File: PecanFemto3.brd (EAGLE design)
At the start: 16.6 x 21.2 mm, 29 parts

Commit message: Added step down converter
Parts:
- added L2: 33uH, PecanPico6:LPS3015
- added L3: 10uH, PecanPico6:LPS3015
- added U$26: 10uF, sven:0805
- added U$27: 100nF, sven:0402
- added U1: TPS62203DBVT, TPS62203:SOT95P280X145-5N
- U$23: value 10uH -> 2.2uF; device PecanPico6:LPS3015 -> sven:0603
- moved U$23 6.59 mm to (13.9, 17.1)
- moved U$14 1.20 mm to (16.4, 15.6)
- moved U$22 0.80 mm to (15.4, 15.6)
- moved U$24 0.61 mm to (11.9, 17.8), turned to 270 degrees
- moved U$16 0.50 mm to (15.7, 17.3)
- moved U$13 0.40 mm to (11.6, 17.9)
- moved U$5 0.10 mm to (13.0, 13.1)
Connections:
- new net N$1: U$23.P$1, U$3.8/V_BCKP
- new net N$15: L3.1_1, L3.1_2, L3.1_3, L3.1_4, L3.1_5, L3.1_6, L3.1_7, L3.1_8, L3.1_9, U1.5
- new net VCC_EN: U$4.16, U1.3
- net GND: now also U$26.P$1, U$27.P$1, U1.2
- net N$14: now also L2.1_1, L2.1_2, L2.1_3, L2.1_4, L2.1_5, L2.1_6, L2.1_7, L2.1_8, L2.1_9; no longer U$23.1_1, U$23.1_2, U$23.1_3, U$23.1_4, U$23.1_5, U$23.1_6, U$23.1_7, U$23.1_8, U$23.1_9
- net VBAT: now also JP1.1, U$23.P$2, U$27.P$2, U$4.19, U1.1
- net VCC: now also L3.2_1, L3.2_2, L3.2_3, L3.2_4, L3.2_5, L3.2_6, L3.2_7, L3.2_8, L3.2_9, U$26.P$2, U1.4; no longer JP1.1, U$3.8/V_BCKP, U$4.19
- net VSOLAR: now also L2.2_1, L2.2_2, L2.2_3, L2.2_4, L2.2_5, L2.2_6, L2.2_7, L2.2_8, L2.2_9; no longer U$23.2_1, U$23.2_2, U$23.2_3, U$23.2_4, U$23.2_5, U$23.2_6, U$23.2_7, U$23.2_8, U$23.2_9
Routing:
- net VCC: track 54.2 -> 38.3 mm
- net VCC_EN: track 0.00 -> 8.71 mm
- net N$15: track 0.00 -> 6.32 mm, vias 0 -> 1
- net VBAT: track 21.0 -> 24.2 mm
- net N$1: track 0.00 -> 1.89 mm
- net VSOLAR: track 26.2 -> 25.4 mm

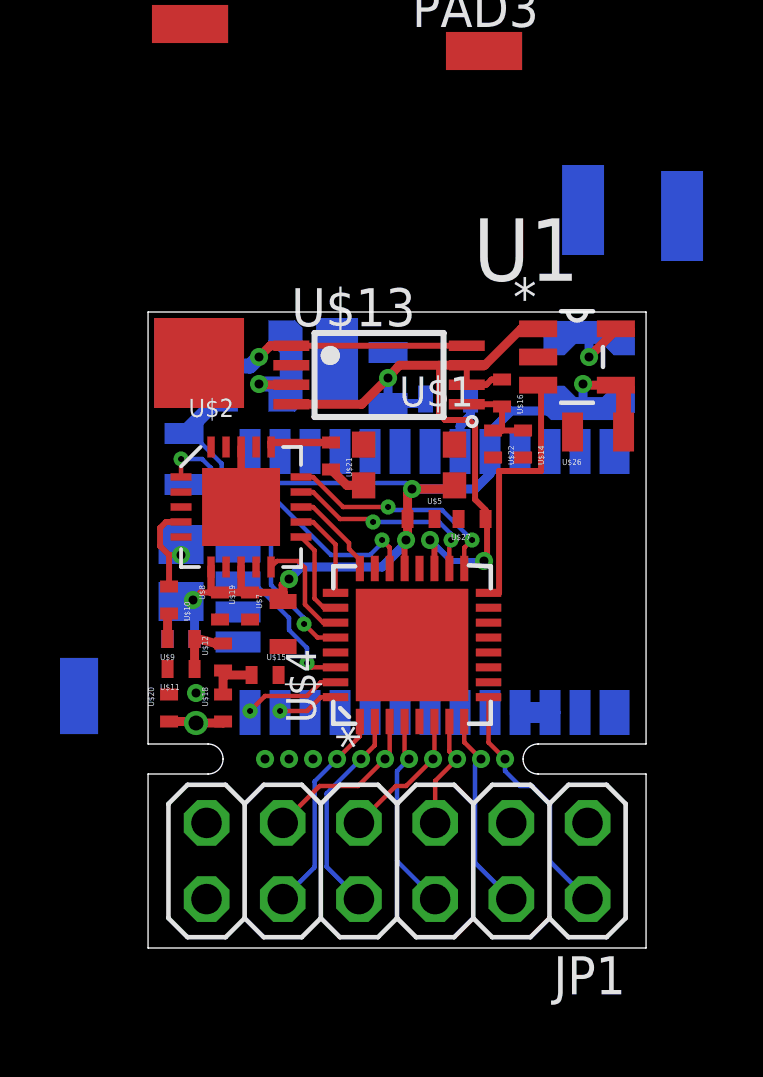
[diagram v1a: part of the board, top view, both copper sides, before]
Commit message: Moved components around
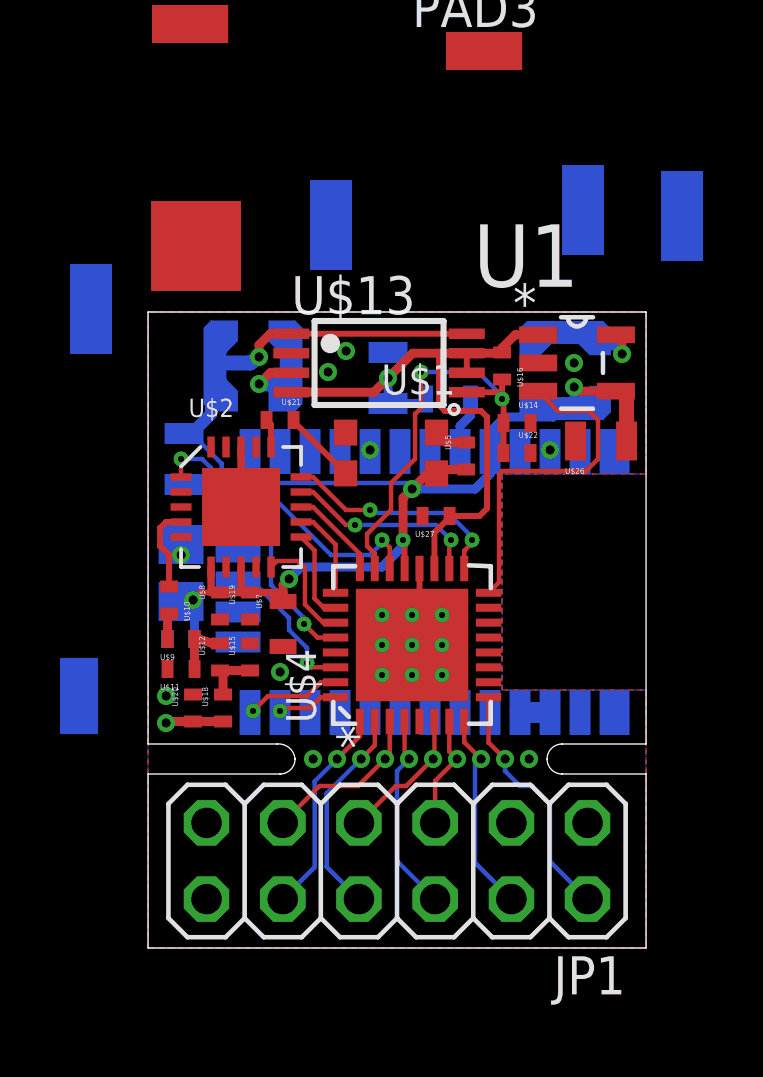
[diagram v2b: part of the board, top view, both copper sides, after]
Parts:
- moved U$5 2.58 mm to (14.5, 15.2), turned to 270 degrees
- moved U$21 2.08 mm to (8.30, 16.4), turned to 180 degrees
- moved U$27 1.20 mm to (13.5, 13.2)
- moved U$16 0.90 mm to (15.7, 18.2)
- moved U$22 0.85 mm to (16.2, 15.3), turned to 180 degrees
- moved L3 0.80 mm to (17.8, 18.1)
- moved U$20 0.80 mm to (5.40, 6.80)
- moved U$15 0.78 mm to (7.30, 8.50), turned to 270 degrees
- moved U$14 0.73 mm to (16.2, 16.3), turned to 180 degrees
- moved U$1 0.72 mm to (12.0, 15.3)
- moved U$13 0.40 mm to (11.6, 18.3)
- moved U$26 0.32 mm to (19.0, 15.7)
- moved U1 0.20 mm to (18.2, 18.3)
- moved U$12 0.10 mm to (6.30, 8.50)
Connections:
- removed net N$17: U$13.5, U$14.P$2, U$16.P$1, U$22.P$2
- new net VBAT_DIFF: U$13.5, U$14.P$2, U$16.P$1, U$22.P$2, U$4.23
- net VBAT: no longer U$4.23
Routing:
- net VBAT_DIFF: track 0.00 -> 14.2 mm, vias 0 -> 2
- net VCC: track 38.3 -> 41.4 mm
- net N$17: track 3.11 -> 0.00 mm
- net GND: track 2.00 -> 4.92 mm, vias 4 -> 18
- net VCC_EN: track 8.71 -> 11.3 mm
- net VBAT: track 24.2 -> 21.8 mm, vias 3 -> 1
- net N$9: track 1.30 -> 2.50 mm
- net N$10: track 2.15 -> 0.96 mm
- net VSOLAR: track 25.4 -> 24.4 mm
- net N$15: track 6.32 -> 6.86 mm
- added copper zone on layer 1, net GND
- added copper zone on layer 16, net GND
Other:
- outline, holes or cut-outs redrawn

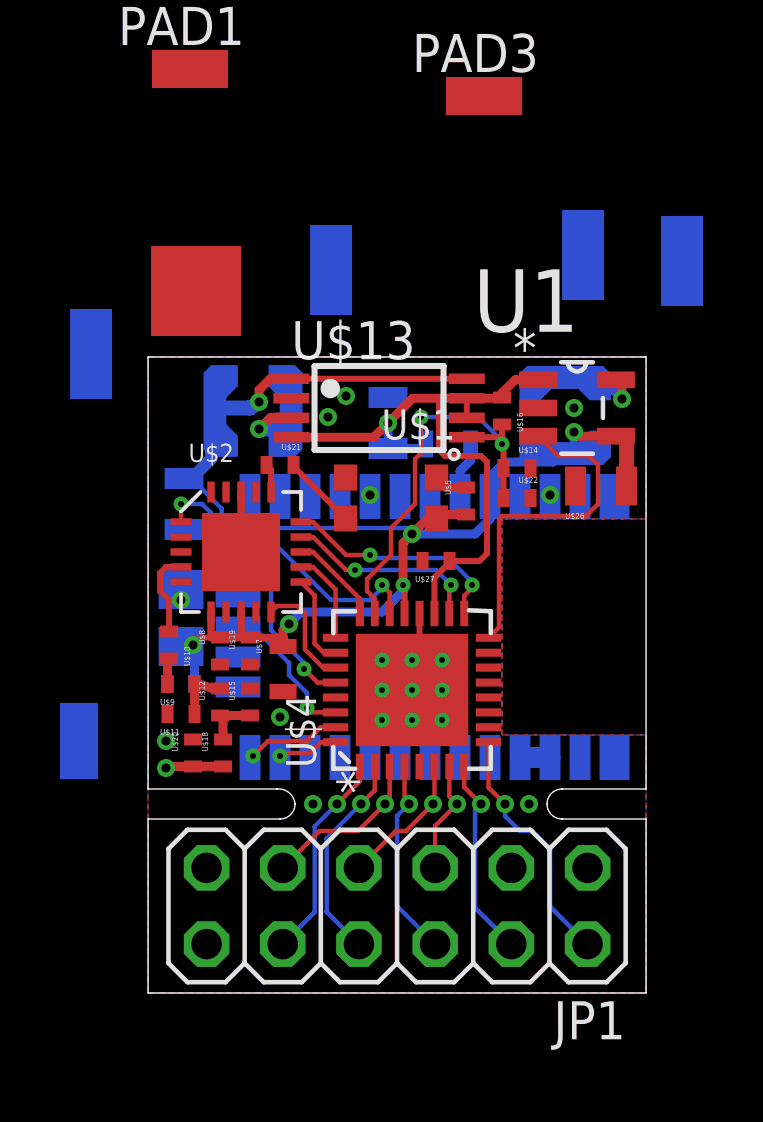
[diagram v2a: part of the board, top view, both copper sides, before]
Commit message: Moved parts around
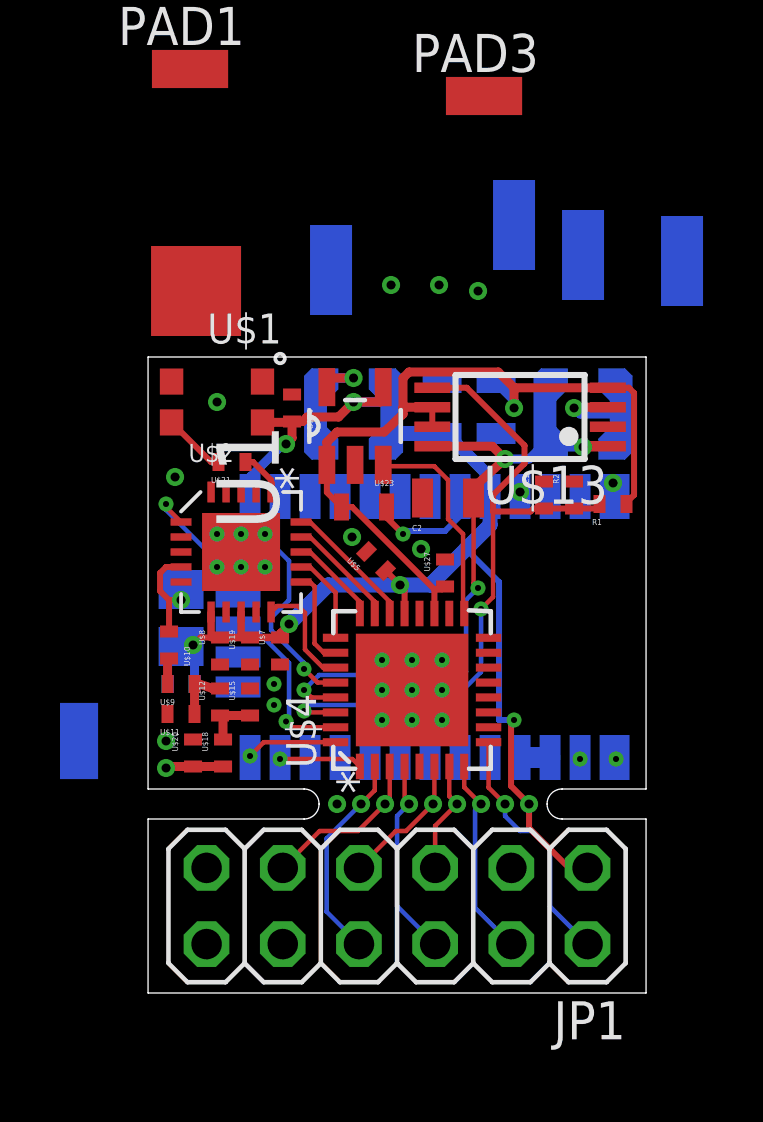
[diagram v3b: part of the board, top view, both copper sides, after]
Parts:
- removed U$16: 22k, PecanPico6:0402
- removed U$17: 22uF, sven:0805
- removed U$22: 10k, PecanPico6:0402
- removed U$24, U$26: 10uF, sven:0805
- added C1: 1nF, sven:0402
- added C2: 22uF, sven:0805
- added C3, C4: 10uF, sven:0805
- added R1: 22k, PecanPico6:0402
- added R2: 10k, PecanPico6:0402
- U$14: value 1nF -> 100nF
- U$7: device sven:0603 -> sven:0402
- moved L2 11.0 mm to (18.4, 18.1)
- moved U$14 7.76 mm to (8.70, 18.3), turned to 90 degrees
- moved U1 7.42 mm to (10.8, 17.7), turned to 90 degrees
- moved L3 7.05 mm to (10.8, 18.1), turned to 180 degrees
- moved U$1 6.62 mm to (6.20, 18.5)
- moved U$13 4.71 mm to (16.3, 18.0), turned to 180 degrees
- moved U$5 3.61 mm to (11.5, 13.2), turned to 315 degrees
- moved U$23 3.50 mm to (11.1, 15.0), flipped to the top, turned to 180 degrees
- moved U$21 1.60 mm to (6.70, 16.5), turned to 0 degrees
- moved U$7 0.61 mm to (8.30, 10.2)
- moved U$27 0.50 mm to (13.8, 12.8), turned to 270 degrees
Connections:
- removed net OUT1: JP1.10, U$4.1
- net CS_RADIO: now also U$4.22; no longer U$4.17
- net GND: now also C1.P$1, C2.P$1, C3.P$1, C4.P$1, JP1.10, R2.P$1, U$14.P$2; no longer U$14.P$1, U$17.P$1, U$22.P$1, U$24.P$1, U$26.P$1
- net MOSI: now also U$4.23; no longer U$4.18
- net RXD: now also U$4.32; no longer U$4.31
- net TIMEPULSE: now also U$4.31; no longer U$4.30
- net TXD: now also U$4.1; no longer U$4.32
- net VBAT: now also C3.P$2, R1.P$2; no longer JP1.1, U$16.P$2, U$24.P$2
- net VBAT_DIFF: now also C1.P$2, R1.P$1, R2.P$2, U$4.30; no longer U$14.P$2, U$16.P$1, U$22.P$2, U$4.23
- net VCC: now also C4.P$2, JP1.1, U$14.P$1; no longer U$26.P$2
- net VCC_EN: now also U$4.17; no longer U$4.16
- net VSOLAR: now also C2.P$2, U$4.29; no longer U$17.P$2, U$4.22
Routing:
- net VBAT_DIFF: track 14.2 -> 23.3 mm
- net VCC: track 41.4 -> 50.2 mm, vias 5 -> 7
- net OUT1: track 6.98 -> 0.00 mm, vias 1 -> 0
- net VBAT: track 21.8 -> 27.2 mm
- net GND: track 4.92 -> 0.35 mm, vias 18 -> 30
- net VCC_EN: track 11.3 -> 7.26 mm
- net CS_RADIO: track 7.69 -> 4.45 mm, vias 2 -> 0
- net MOSI: track 6.64 -> 3.74 mm, vias 2 -> 0
- net N$1: track 1.89 -> 3.93 mm, vias 0 -> 1
- net RADIO_SDN: track 9.91 -> 11.4 mm
- net VSOLAR: track 24.4 -> 25.7 mm, vias 2 -> 4
- net TIMEPULSE: track 4.96 -> 5.92 mm
- net TXD: track 2.09 -> 2.81 mm
- net N$10: track 0.96 -> 1.50 mm
- removed copper zone on layer 1, net GND
- removed copper zone on layer 16, net GND
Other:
- outline, holes or cut-outs redrawn

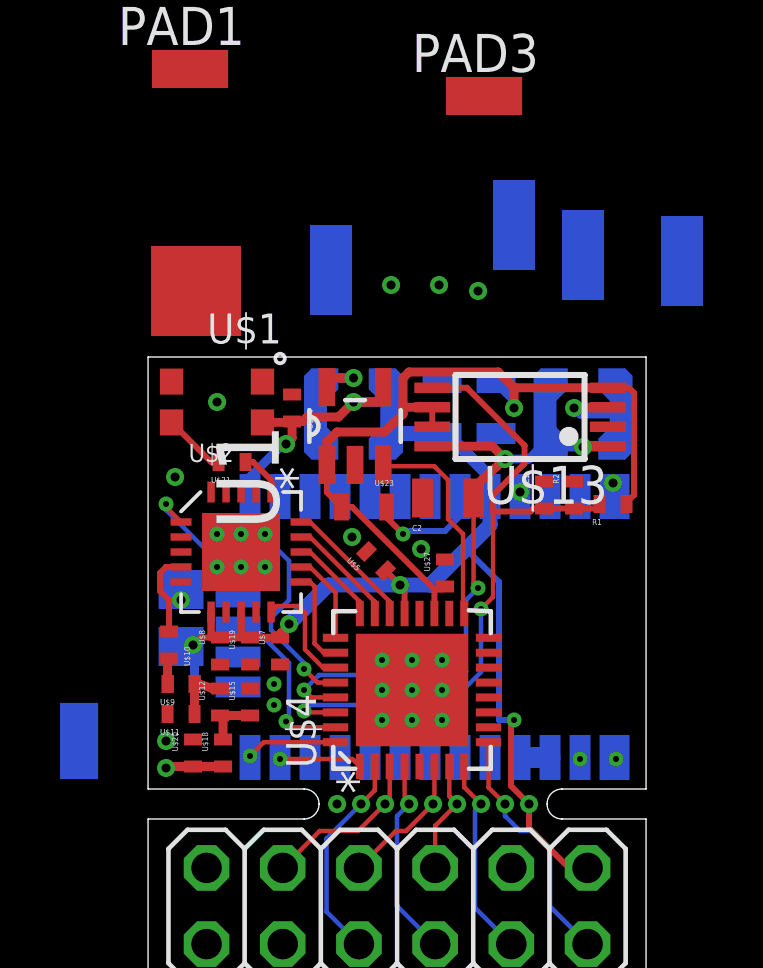
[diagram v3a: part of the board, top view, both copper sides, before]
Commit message: Moved parts around, added MOSFET switch for GPS
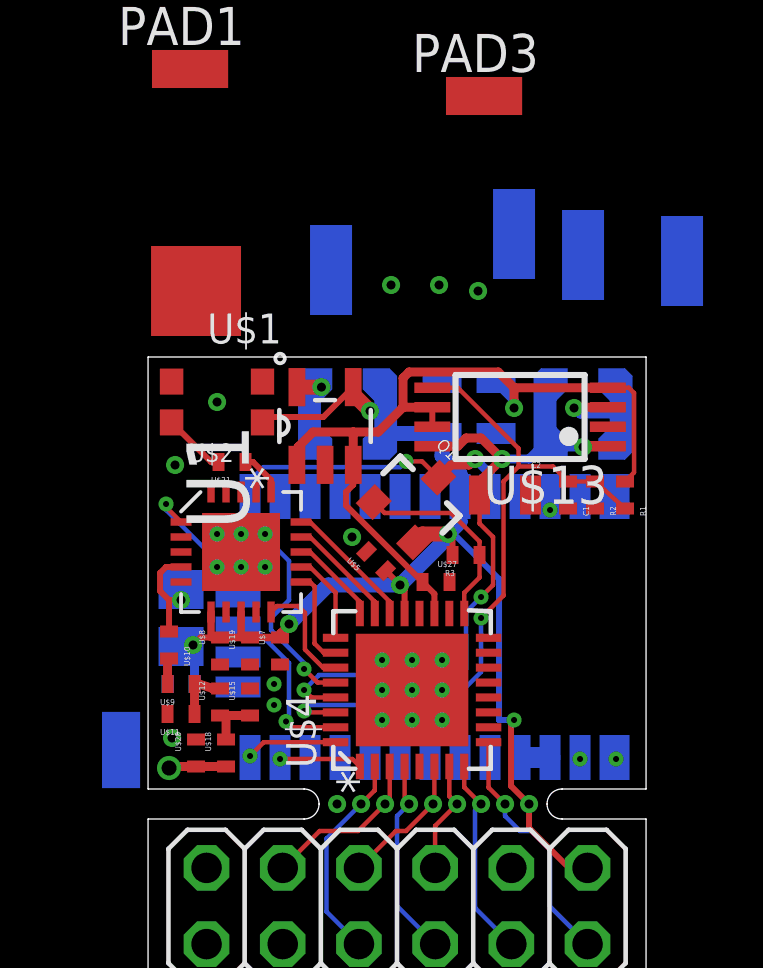
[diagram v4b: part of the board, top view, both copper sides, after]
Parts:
- removed U$14: 100nF, sven:0402
- removed U$23: 2.2uF, sven:0603
- added Q1: AP2301, PecanPico6:SOT23-3
- added R3: 47k, PecanPico6:0402
- moved C2 1.90 mm to (15.8, 15.4), turned to 180 degrees
- moved PAD2 1.43 mm to (3.00, 6.90)
- moved U1 1.00 mm to (9.80, 17.7)
- moved C1 0.80 mm to (17.9, 15.4), turned to 90 degrees
- moved R2 0.70 mm to (18.8, 15.4), turned to 90 degrees
- moved R1 0.50 mm to (19.8, 15.4), turned to 90 degrees
- moved U$27 0.42 mm to (13.5, 12.5), turned to 180 degrees
- moved L3 0.20 mm to (10.6, 18.1)
- moved U$18 0.10 mm to (6.50, 6.80)
- moved U$20 0.10 mm to (5.50, 6.80)
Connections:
- removed net N$1: U$23.P$1, U$3.8/V_BCKP
- removed net VCC_EN: U$4.17, U1.3
- new net GPS_OFF: Q1.1, R3.P$2, U$4.17
- new net N$16: Q1.3, U$3.1/VCC_IO, U$3.9/VCC
- net GND: now also U$4.18; no longer U$14.P$2
- net VBAT: now also U1.3; no longer U$23.P$2
- net VCC: now also Q1.2, R3.P$1, U$3.8/V_BCKP; no longer U$14.P$1, U$3.1/VCC_IO, U$3.9/VCC
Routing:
- net N$16: track 0.00 -> 10.2 mm, vias 0 -> 2
- net VCC_EN: track 7.26 -> 0.00 mm
- net GPS_OFF: track 0.00 -> 6.68 mm
- net N$1: track 3.93 -> 0.00 mm, vias 1 -> 0
- net VCC: track 50.2 -> 47.8 mm
- net N$15: track 7.33 -> 6.66 mm
- net GND: vias 30 -> 28
